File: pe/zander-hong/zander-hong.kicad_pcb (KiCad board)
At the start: 2 copper layers, 18.8 x 16.3 mm, 8 parts, among them U1 AP62300TWU

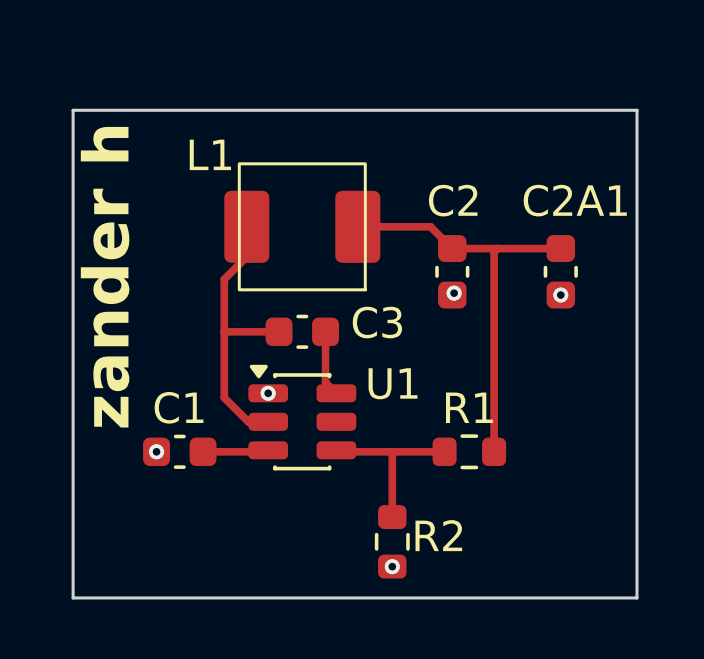
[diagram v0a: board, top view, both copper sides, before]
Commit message: changed enable high voltage from 12v to 5v
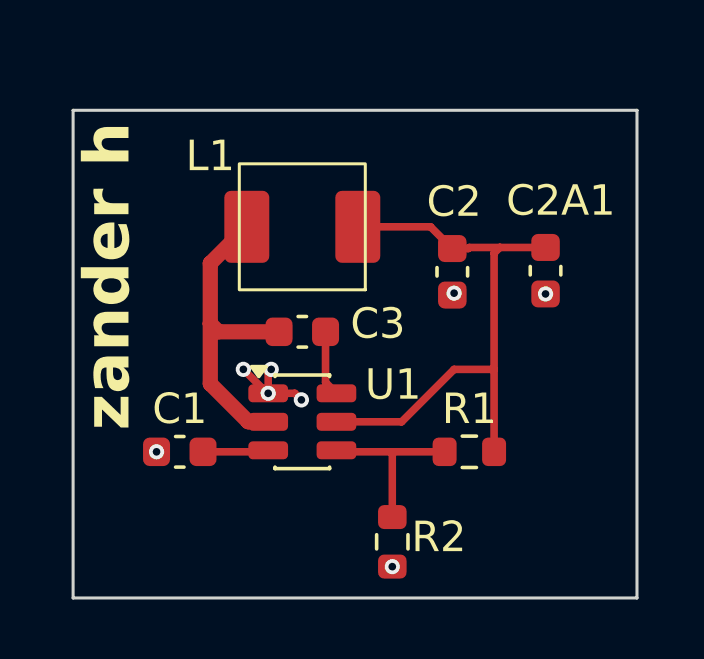
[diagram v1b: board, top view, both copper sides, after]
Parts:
- moved C2A1 0.51 mm to (165.6, 108.0)
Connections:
- U1 pad 5: +12V -> Vout
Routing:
- net Vout: track 13.8 -> 19.9 mm
- net GND: track 0.34 -> 3.35 mm, vias 5 -> 8
- net Net-(U1-SW): track 9.63 -> 11.6 mm
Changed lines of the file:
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@@
 		(capping no)
 		(filling no)
-		(zone_defaults)
 		(pcbplotparams
 			(layerselection 0x00000000_00000000_55555555_5755f5ff)
@@
 			(layers "F.Cu" "F.Mask" "F.Paste")
 			(roundrect_rratio 0.25)
-			(net "+12V")
+			(net "Vout")
 			(pinfunction "EN_5")
 			(pintype "passive")
@@
 	(footprint "Capacitor_SMD:C_0603_1608Metric"
 		(layer "F.Cu")
-		(at 166.116 108 -90)
+		(at 165.608 107.963 -90)
 		(descr "Capacitor SMD 0603 (1608 Metric), square (rectangular) end terminal, IPC-7351 nominal, (Body size source: IPC-SM-782 page 76, https://www.pcb-3d.com/wordpress/wp-content/uploads/ipc-sm-782a_amendment_1_and_2.pdf)")
 		(tags "capacitor")
@@
 	)
 	(segment
+		(start 156.333 112.05)
+		(end 155.535 111.252)
+		(width 0.254)
+		(layer "F.Cu")
+		(net "GND")
+	)
+	(segment
 		(start 160.5 117.825)
 		(end 160.5 117.828)
@@
 	)
 	(segment
-		(start 166.116 108.775)
-		(end 166.053 108.775)
-		(width 0.254)
-		(layer "F.Cu")
-		(net "GND")
-	)
-	(segment
-		(start 166 108.775)
-		(end 166.053 108.775)
+		(start 156.3625 112.05)
+		(end 156.3625 111.3535)
+		(width 0.254)
+		(layer "F.Cu")
+		(net "GND")
+	)
+	(segment
+		(start 157.251161 112.05)
+		(end 157.469872 112.268711)
+		(width 0.254)
+		(layer "F.Cu")
+		(net "GND")
+	)
+	(segment
+		(start 156.3625 112.05)
+		(end 157.251161 112.05)
+		(width 0.254)
+		(layer "F.Cu")
+		(net "GND")
+	)
+	(segment
+		(start 156.3625 112.05)
+		(end 156.333 112.05)
+		(width 0.254)
+		(layer "F.Cu")
+		(net "GND")
+	)
+	(segment
+		(start 156.3625 111.3535)
+		(end 156.464 111.252)
+		(width 0.254)
+		(layer "F.Cu")
+		(net "GND")
+	)
+	(segment
+		(start 165.608 108.712)
+		(end 165.608 108.738)
 		(width 0.254)
 		(layer "F.Cu")
@@
 		(width 0.254)
 		(layer "F.Cu")
+		(net "GND")
+	)
+	(via
+		(at 155.535 111.252)
+		(size 0.508)
+		(drill 0.254)
+		(layers "F.Cu" "B.Cu")
+		(free yes)
 		(net "GND")
 	)
@@
 	)
 	(via
-		(at 166.116 108.775)
-		(size 0.508)
-		(drill 0.254)
-		(layers "F.Cu" "B.Cu")
-		(net "GND")
-	)
-	(via
 		(at 152.641 114)
 		(size 0.508)
@@
 	)
 	(via
+		(at 156.464 111.252)
+		(size 0.508)
+		(drill 0.254)
+		(layers "F.Cu" "B.Cu")
+		(free yes)
+		(net "GND")
+	)
+	(via
 		(at 156.3625 112.05)
 		(size 0.508)
@@
 		(net "GND")
 	)
-	(segment
-		(start 166.053 108.775)
-		(end 166.116 108.712)
-		(width 0.254)
-		(layer "B.Cu")
-		(net "GND")
-	)
-	(segment
-		(start 154.9 108.25)
-		(end 154.9 110)
-		(width 0.254)
+	(via
+		(at 157.469872 112.268711)
+		(size 0.508)
+		(drill 0.254)
+		(layers "F.Cu" "B.Cu")
+		(free yes)
+		(net "GND")
+	)
+	(via
+		(at 165.608 108.738)
+		(size 0.508)
+		(drill 0.254)
+		(layers "F.Cu" "B.Cu")
+		(net "GND")
+	)
+	(segment
+		(start 154.432 111.731999)
+		(end 154.432 109.728)
+		(width 0.508)
 		(layer "F.Cu")
 		(net "Net-(U1-SW)")
@@
 	(segment
 		(start 155.700001 113)
-		(end 156.3625 113)
-		(width 0.254)
+		(end 154.432 111.731999)
+		(width 0.508)
+		(layer "F.Cu")
+		(net "Net-(U1-SW)")
+	)
+	(segment
+		(start 154.432 107.718)
+		(end 155.65 106.5)
+		(width 0.508)
+		(layer "F.Cu")
+		(net "Net-(U1-SW)")
+	)
+	(segment
+		(start 154.432 109.728)
+		(end 154.432 107.718)
+		(width 0.508)
 		(layer "F.Cu")
 		(net "Net-(U1-SW)")
@@
 	)
 	(segment
-		(start 154.9 112.199999)
+		(start 156.3625 113)
 		(end 155.700001 113)
-		(width 0.254)
+		(width 0.508)
 		(layer "F.Cu")
 		(net "Net-(U1-SW)")
 	)
 	(segment
-		(start 156.725 110)
-		(end 154.9 110)
-		(width 0.254)
+		(start 154.432 109.728)
+		(end 154.704 110)
+		(width 0.508)
 		(layer "F.Cu")
 		(net "Net-(U1-SW)")
 	)
 	(segment
-		(start 154.9 110)
-		(end 154.9 112.199999)
-		(width 0.254)
-		(layer "F.Cu")
-		(net "Net-(U1-SW)")
-	)
-	(segment
-		(start 155.65 107.5)
-		(end 154.9 108.25)
-		(width 0.254)
+		(start 154.704 110)
+		(end 156.725 110)
+		(width 0.508)
 		(layer "F.Cu")
 		(net "Net-(U1-SW)")
@@
 	)
 	(segment
-		(start 164 107.225)
-		(end 162.5 107.225)
+		(start 163.893 107.379)
+		(end 164.084 107.188)
 		(width 0.254)
 		(layer "F.Cu")
@@
 	)
 	(segment
-		(start 163.893 107.332)
-		(end 164 107.225)
+		(start 163.068 107.188)
+		(end 164.084 107.188)
 		(width 0.254)
 		(layer "F.Cu")
@@
 	)
 	(segment
+		(start 160.812 113)
+		(end 162.56 111.252)
+		(width 0.254)
+		(layer "F.Cu")
+		(net "Vout")
+	)
+	(segment
+		(start 162.56 111.252)
+		(end 163.893 111.252)
+		(width 0.254)
+		(layer "F.Cu")
+		(net "Vout")
+	)
+	(segment
+		(start 158.169896 113)
+		(end 158.6375 113)
+		(width 0.254)
+		(layer "F.Cu")
+		(net "Vout")
+	)
+	(segment
+		(start 158.6375 113)
+		(end 160.812 113)
+		(width 0.254)
+		(layer "F.Cu")
+		(net "Vout")
+	)
+	(segment
+		(start 162.5 107.225)
+		(end 163.031 107.225)
+		(width 0.254)
+		(layer "F.Cu")
+		(net "Vout")
+	)
+	(segment
 		(start 163.893 114)
-		(end 163.893 107.332)
+		(end 163.893 111.252)
 		(width 0.254)
 		(layer "F.Cu")
@@
 	)
 	(segment
-		(start 166 107.225)
-		(end 164 107.225)
-		(width 0.254)
-		(layer "F.Cu")
+		(start 164.084 107.188)
+		(end 165.608 107.188)
+		(width 0.254)
+		(layer "F.Cu")
+		(net "Vout")
+	)
+	(segment
+		(start 163.031 107.225)
+		(end 163.068 107.188)
+		(width 0.254)
+		(layer "F.Cu")
+		(net "Vout")
+	)
+	(segment
+		(start 163.893 111.252)
+		(end 163.893 107.379)
+		(width 0.254)
+		(layer "F.Cu")

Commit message: changes in schematic formatting and footprints along with enable no connect
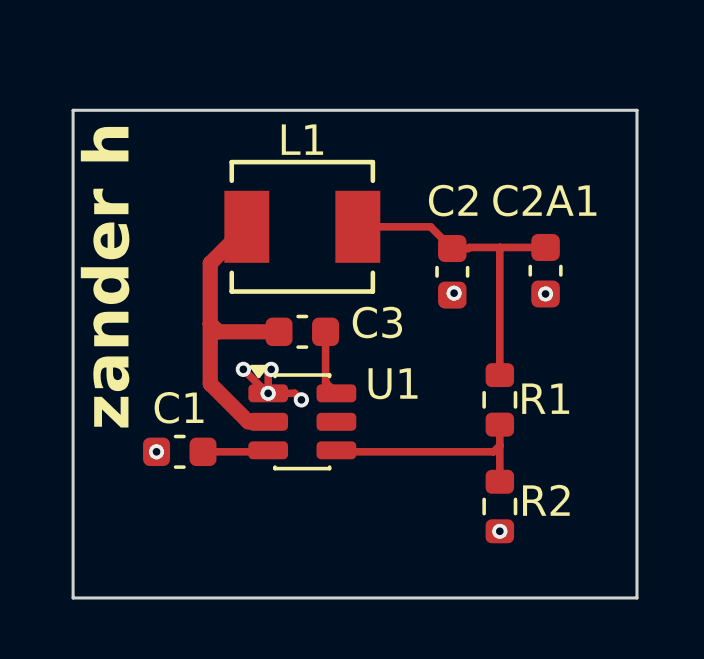
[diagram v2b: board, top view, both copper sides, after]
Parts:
- L1: footprint Inductor_SMD:L_SRP4020TA -> inductor_SRP4020:IND_SRP4020_BRN
- moved R2 3.77 mm to (164.1, 115.8)
- moved R1 2.01 mm to (164.1, 112.3), turned to 90 degrees
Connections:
- U1 pad 5: Vout -> unconnected-(U1-EN-Pad5)
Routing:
- net Vout: track 19.9 -> 10.8 mm
- net Net-(U1-FB): track 5.80 -> 7.46 mm

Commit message: updated pcb to align with datasheet requirements for component placement
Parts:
- moved R1 1.52 mm to (162.6, 112.3)
- moved R2 1.52 mm to (162.6, 115.8)
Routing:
- net Net-(U1-FB): track 7.46 -> 5.96 mm
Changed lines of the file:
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@@
 	(footprint "Resistor_SMD:R_0603_1608Metric"
 		(layer "F.Cu")
-		(at 164.084 115.824 -90)
+		(at 162.56 115.824 -90)
 		(descr "Resistor SMD 0603 (1608 Metric), square (rectangular) end terminal, IPC-7351 nominal, (Body size source: IPC-SM-782 page 72, https://www.pcb-3d.com/wordpress/wp-content/uploads/ipc-sm-782a_amendment_1_and_2.pdf)")
 		(tags "resistor")
@@
 		)
 		(property "Value" "R"
-			(at 0 1.43 180)
+			(at -1.016 1.43 180)
 			(layer "F.Fab")
 			(effects
@@
 		)
 		(property "Value" "C"
-			(at 0 1.43 0)
+			(at -2.052 -0.78 0)
 			(layer "F.Fab")
 			(effects
@@
 	(footprint "Resistor_SMD:R_0603_1608Metric"
 		(layer "F.Cu")
-		(at 164.084 112.268 90)
+		(at 162.56 112.268 90)
 		(descr "Resistor SMD 0603 (1608 Metric), square (rectangular) end terminal, IPC-7351 nominal, (Body size source: IPC-SM-782 page 72, https://www.pcb-3d.com/wordpress/wp-content/uploads/ipc-sm-782a_amendment_1_and_2.pdf)")
 		(tags "resistor")
@@
 		)
 		(property "Value" "R"
-			(at 0 -1.524 180)
+			(at -1.016 -1.524 180)
 			(layer "F.Fab")
 			(effects
@@
 	)
 	(via
-		(at 164.084 116.649)
+		(at 162.56 116.649)
 		(size 0.508)
 		(drill 0.254)
@@
 	)
 	(segment
-		(start 164.084 113.792)
-		(end 164.084 114.999)
+		(start 162.56 113.093)
+		(end 162.56 113.792)
 		(width 0.254)
 		(layer "F.Cu")
@@
 	)
 	(segment
-		(start 164.084 113.093)
-		(end 164.084 113.792)
+		(start 158.6375 113.95)
+		(end 162.402 113.95)
+		(width 0.254)
+		(layer "F.Cu")
+		(net "Net-(U1-FB)")
+	)
+	(segment
+		(start 162.402 113.95)
+		(end 162.56 113.792)
 		(width 0.254)
 		(layer "F.Cu")
@@
 	)
 	(segment
-		(start 163.876 114)
-		(end 164.084 113.792)
-		(width 0.254)
-		(layer "F.Cu")
-		(net "Net-(U1-FB)")
-	)
-	(segment
-		(start 158.6875 114)
-		(end 163.876 114)
+		(start 162.56 113.792)
+		(end 162.56 114.999)
 		(width 0.254)
 		(layer "F.Cu")
@@
 	(segment
 		(start 163.068 107.188)
+		(end 163.576 107.188)
+		(width 0.254)
+		(layer "F.Cu")
+		(net "Vout")
+	)
+	(segment
+		(start 163.576 107.188)
 		(end 164.084 107.188)
+		(width 0.254)
+		(layer "F.Cu")
+		(net "Vout")
+	)
+	(segment
+		(start 162.56 110.744)
+		(end 163.576 109.728)
 		(width 0.254)
 		(layer "F.Cu")
@@
 	)
 	(segment
-		(start 164.084 107.188)
-		(end 164.084 111.443)
-		(width 0.254)
-		(layer "F.Cu")
+		(start 162.56 111.443)
+		(end 162.56 110.744)
+		(width 0.254)
+		(layer "F.Cu")
+		(net "Vout")
+	)
+	(segment
+		(start 163.576 109.728)
+		(end 163.576 107.188)
+		(width 0.254)
+		(layer "F.Cu")
